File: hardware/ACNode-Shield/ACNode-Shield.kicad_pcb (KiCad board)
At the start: 2 copper layers, 50 x 50 mm, 15 parts, among them J1 MICRO_SD_HINGE, P1 CONN_NFC, P2 CONN_RELAY, P3 CONN_RGB_LED, P4 CONN_X6, P5 CONN_X7, P6 CONN_WS2812, Q1 PN2222A, SW1 SW_RST, SW2 SW_BTN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

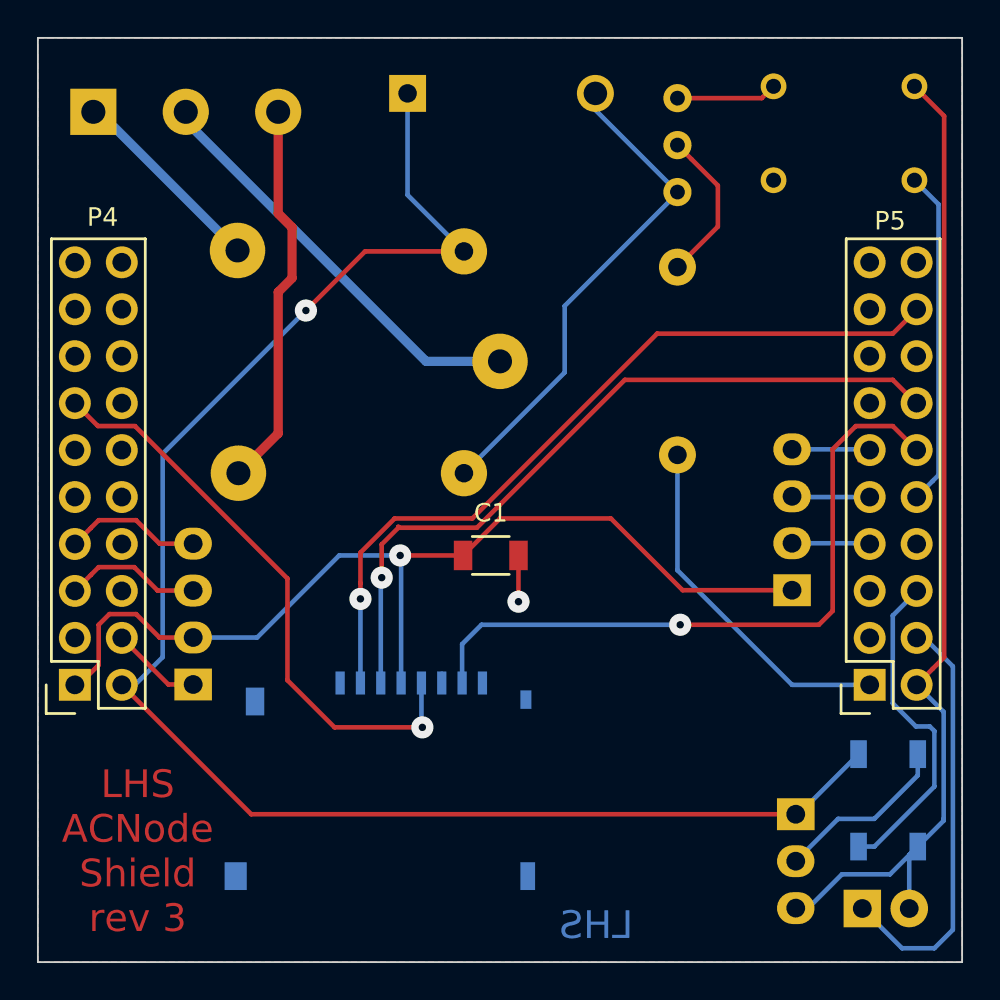
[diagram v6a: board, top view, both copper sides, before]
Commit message: Reversed contacts on the SD card connector - it should work now.
Bumped revision of the board to 4.
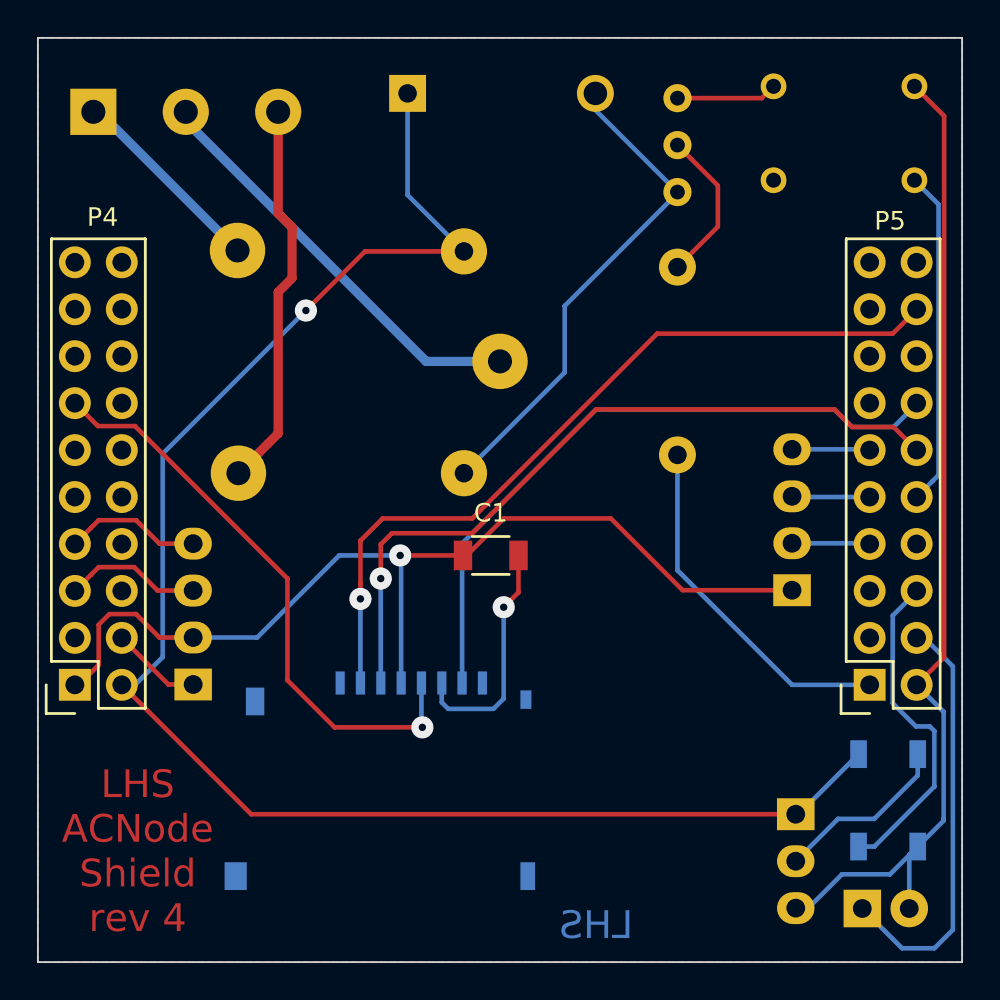
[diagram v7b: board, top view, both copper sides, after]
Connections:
- J1 pad 3: PQ3 -> PQ2
- J1 pad 7: PQ2 -> PQ3
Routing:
- net GND: track 69.8 -> 80.1 mm
- net PQ3: track 42.2 -> 36.1 mm, vias 1 -> 0
- net PQ2: track 37.2 -> 41.8 mm
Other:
- board text added: "LHS ACNode Shield rev 4"
- board text removed: "LHS ACNode Shield rev 3"
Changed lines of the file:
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@@
     (thickness 1.6)
     (drawings 6)
-    (tracks 174)
+    (tracks 176)
     (zones 0)
     (modules 15)
@@
       (net 9 PQ1))
     (pad 3 smd rect (at -3.55 7.1) (size 0.5 1.25) (layers B.Cu B.Paste B.Mask)
-      (net 8 PQ3))
+      (net 6 PQ2))
     (pad 4 smd rect (at -4.65 7.1) (size 0.5 1.25) (layers B.Cu B.Paste B.Mask)
       (net 1 +3.3v))
@@
       (net 2 GND))
     (pad 7 smd rect (at -7.95 7.1) (size 0.5 1.25) (layers B.Cu B.Paste B.Mask)
-      (net 6 PQ2))
+      (net 8 PQ3))
     (pad 8 smd rect (at -9.05 7.1) (size 0.5 1.25) (layers B.Cu B.Paste B.Mask)
       (net 5 "Net-(J1-Pad8)"))
@@
     )
   )
-  (gr_text "LHS\nACNode\nShield\nrev 3" (at 17.4 56) (layer F.Cu)
+  (gr_text "LHS\nACNode\nShield\nrev 4" (at 17.4 56) (layer F.Cu)
     (effects (font (size 1.5 1.5) (thickness 0.3)))
   )
@@
   (segment (start 23.86 44.44) (end 28.3 40) (width 0.25) (layer B.Cu) (net 1))
   (segment (start 28.3 40) (end 31.6 40) (width 0.25) (layer B.Cu) (net 1))
-  (segment (start 31.6 40) (end 35 40) (width 0.25) (layer F.Cu) (net 1))
+  (segment (start 31.6 40) (end 35.2 40) (width 0.25) (layer F.Cu) (net 1))
   (via (at 31.6 40) (size 1.2) (drill 0.4) (layers F.Cu B.Cu) (net 1))
   (segment (start 20.4 44.44) (end 20.56 44.44) (width 0.25) (layer B.Cu) (net 1))
   (segment (start 52.8 41.88) (end 46.88 41.88) (width 0.25) (layer F.Cu) (net 1))
   (segment (start 46.88 41.88) (end 43 38) (width 0.25) (layer F.Cu) (net 1))
-  (segment (start 43 38) (end 37 38) (width 0.25) (layer F.Cu) (net 1))
-  (segment (start 37 38) (end 35 40) (width 0.25) (layer F.Cu) (net 1))
+  (segment (start 43 38) (end 37.2 38) (width 0.25) (layer F.Cu) (net 1))
+  (segment (start 37.2 38) (end 35.2 40) (width 0.25) (layer F.Cu) (net 1))
   (segment (start 31.65 46.9) (end 31.65 46.35) (width 0.25) (layer B.Cu) (net 1))
   (segment (start 20.4 44.44) (end 18.57913 44.44) (width 0.25) (layer F.Cu) (net 1))
@@
   (segment (start 15.288601 45.924999) (end 14.2136 47) (width 0.25) (layer F.Cu) (net 1))
   (segment (start 14.2136 47) (end 14 47) (width 0.25) (layer F.Cu) (net 1))
-  (segment (start 38 42.5) (end 38 40) (width 0.25) (layer F.Cu) (net 2))
-  (via (at 38 42.5) (size 1.2) (drill 0.4) (layers F.Cu B.Cu) (net 2))
+  (segment (start 33.85 46.9) (end 33.85 47.95) (width 0.25) (layer B.Cu) (net 2))
+  (segment (start 38 42) (end 38 40) (width 0.25) (layer F.Cu) (net 2))
+  (segment (start 37.2 42.8) (end 38 42) (width 0.25) (layer F.Cu) (net 2))
+  (via (at 37.2 42.8) (size 1.2) (drill 0.4) (layers F.Cu B.Cu) (net 2))
+  (segment (start 37.2 47.75) (end 37.2 42.8) (width 0.25) (layer B.Cu) (net 2))
+  (segment (start 36.65 48.3) (end 37.2 47.75) (width 0.25) (layer B.Cu) (net 2))
+  (segment (start 34.2 48.3) (end 36.65 48.3) (width 0.25) (layer B.Cu) (net 2))
+  (segment (start 33.85 47.95) (end 34.2 48.3) (width 0.25) (layer B.Cu) (net 2))
   (segment (start 33.85 46.9) (end 33.85 46.4) (width 0.25) (layer B.Cu) (net 2))
   (segment (start 53 59.08) (end 52.58 59.08) (width 0.25) (layer B.Cu) (net 2))
@@
   (segment (start 53 54) (end 53.15044 54) (width 0.25) (layer B.Cu) (net 4))
   (segment (start 53.15044 54) (end 56.3998 50.75064) (width 0.25) (layer B.Cu) (net 4))
-  (segment (start 34.95 46.9) (end 34.95 44.8) (width 0.25) (layer B.Cu) (net 6))
-  (segment (start 58.25 33) (end 56.25 33) (width 0.25) (layer F.Cu) (net 6))
-  (segment (start 56.25 33) (end 55 34.25) (width 0.25) (layer F.Cu) (net 6))
-  (segment (start 55 34.25) (end 55 43) (width 0.25) (layer F.Cu) (net 6))
-  (segment (start 55 43) (end 54.25 43.75) (width 0.25) (layer F.Cu) (net 6))
-  (segment (start 54.25 43.75) (end 46.75 43.75) (width 0.25) (layer F.Cu) (net 6))
-  (segment (start 58.25 33) (end 59.54 34.29) (width 0.25) (layer F.Cu) (net 6))
-  (via (at 46.75 43.75) (size 1.2) (drill 0.4) (layers F.Cu B.Cu) (net 6))
-  (segment (start 36 43.75) (end 46.75 43.75) (width 0.25) (layer B.Cu) (net 6))
-  (segment (start 34.95 44.8) (end 36 43.75) (width 0.25) (layer B.Cu) (net 6))
+  (segment (start 30.55 46.9) (end 30.55 41.25) (width 0.25) (layer B.Cu) (net 6))
+  (segment (start 58.29 33.05) (end 59.54 34.3) (width 0.25) (layer F.Cu) (net 6))
+  (segment (start 56.05 33.05) (end 58.29 33.05) (width 0.25) (layer F.Cu) (net 6))
+  (segment (start 55.1 32.1) (end 56.05 33.05) (width 0.25) (layer F.Cu) (net 6))
+  (segment (start 42.2 32.1) (end 55.1 32.1) (width 0.25) (layer F.Cu) (net 6))
+  (segment (start 35.5 38.8) (end 42.2 32.1) (width 0.25) (layer F.Cu) (net 6))
+  (segment (start 31.15 38.8) (end 35.5 38.8) (width 0.25) (layer F.Cu) (net 6))
+  (segment (start 30.55 39.4) (end 31.15 38.8) (width 0.25) (layer F.Cu) (net 6))
+  (segment (start 30.55 40) (end 30.55 39.4) (width 0.25) (layer F.Cu) (net 6))
+  (segment (start 30.55 41.25) (end 30.55 40) (width 0.25) (layer F.Cu) (net 6))
+  (via (at 30.55 41.25) (size 1.2) (drill 0.4) (layers F.Cu B.Cu) (net 6))
   (segment (start 59.54 34.3) (end 59.54 34.29) (width 0.25) (layer F.Cu) (net 6))
+  (segment (start 30.55 46.45) (end 30.55 46.9) (width 0.25) (layer B.Cu) (net 6))
+  (segment (start 30.55 46.9) (end 30.55 46.45) (width 0.25) (layer B.Cu) (net 6))
+  (segment (start 30.55 46.9) (end 30.55 46.4) (width 0.25) (layer B.Cu) (net 6))
   (segment (start 32.8 49.3) (end 28.05 49.3) (width 0.25) (layer F.Cu) (net 7))
   (segment (start 25.5 41.25) (end 25.5 46.75) (width 0.25) (layer F.Cu) (net 7))
@@
   (segment (start 32.75 47.25) (end 32.75 46.9) (width 0.25) (layer B.Cu) (net 7))
   (segment (start 32.75 46.9) (end 32.75 46.5) (width 0.25) (layer B.Cu) (net 7))
-  (segment (start 30.55 46.9) (end 30.55 41.25) (width 0.25) (layer B.Cu) (net 8))
-  (segment (start 30.6 39.4) (end 31.5 38.5) (width 0.25) (layer F.Cu) (net 8))
-  (segment (start 30.6 41.2) (end 30.6 39.4) (width 0.25) (layer F.Cu) (net 8))
-  (via (at 30.6 41.2) (size 1.2) (drill 0.4) (layers F.Cu B.Cu) (net 8))
-  (segment (start 30.55 41.25) (end 30.6 41.2) (width 0.25) (layer B.Cu) (net 8))
-  (segment (start 31.5 38.5) (end 31.5 38.450002) (width 0.25) (layer F.Cu) (net 8))
-  (segment (start 31.5 38.450002) (end 31.5 38.5) (width 0.25) (layer F.Cu) (net 8))
-  (segment (start 35.75 38.5) (end 31.5 38.5) (width 0.25) (layer F.Cu) (net 8))
-  (segment (start 59.51 31.76) (end 58.25 30.5) (width 0.25) (layer F.Cu) (net 8))
-  (segment (start 58.25 30.5) (end 43.75 30.5) (width 0.25) (layer F.Cu) (net 8))
-  (segment (start 43.75 30.5) (end 35.75 38.5) (width 0.25) (layer F.Cu) (net 8))
-  (segment (start 31.5 38.5) (end 31.5 38.5) (width 0.25) (layer F.Cu) (net 8))
-  (segment (start 30.55 46.45) (end 30.55 46.9) (width 0.25) (layer B.Cu) (net 8))
-  (segment (start 30.55 46.9) (end 30.55 46.45) (width 0.25) (layer B.Cu) (net 8))
+  (segment (start 59.54 31.76) (end 59.54 31.81) (width 0.25) (layer B.Cu) (net 8))
+  (segment (start 59.54 31.81) (end 58.3 33.05) (width 0.25) (layer B.Cu) (net 8))
+  (segment (start 34.95 39.35) (end 34.95 46.9) (width 0.25) (layer B.Cu) (net 8))
+  (segment (start 42.2 32.1) (end 34.95 39.35) (width 0.25) (layer B.Cu) (net 8))
+  (segment (start 55.1 32.1) (end 42.2 32.1) (width 0.25) (layer B.Cu) (net 8))
+  (segment (start 56.05 33.05) (end 55.1 32.1) (width 0.25) (layer B.Cu) (net 8))
+  (segment (start 58.3 33.05) (end 56.05 33.05) (width 0.25) (layer B.Cu) (net 8))
   (segment (start 59.54 31.76) (end 59.51 31.76) (width 0.25) (layer F.Cu) (net 8))
-  (segment (start 30.55 46.9) (end 30.55 46.4) (width 0.25) (layer B.Cu) (net 8))
-  (segment (start 31.3 38) (end 29.45 39.85) (width 0.25) (layer F.Cu) (net 9))
+  (segment (start 30.65 38) (end 29.45 39.2) (width 0.25) (layer F.Cu) (net 9))
   (segment (start 29.45 42.35) (end 29.45 41.501472) (width 0.25) (layer F.Cu) (net 9))
-  (segment (start 29.45 41.501472) (end 29.45 39.85) (width 0.25) (layer F.Cu) (net 9))
+  (segment (start 29.45 41.501472) (end 29.45 39.2) (width 0.25) (layer F.Cu) (net 9))
   (segment (start 29.45 46.9) (end 29.45 42.35) (width 0.25) (layer B.Cu) (net 9))
   (via (at 29.45 42.35) (size 1.2) (drill 0.4) (layers F.Cu B.Cu) (net 9))
   (segment (start 58.25 28) (end 45.5 28) (width 0.25) (layer F.Cu) (net 9))
   (segment (start 45.5 28) (end 35.5 38) (width 0.25) (layer F.Cu) (net 9))
-  (segment (start 35.5 38) (end 31.3 38) (width 0.25) (layer F.Cu) (net 9))
+  (segment (start 35.5 38) (end 30.65 38) (width 0.25) (layer F.Cu) (net 9))
   (segment (start 59.54 26.71) (end 58.25 28) (width 0.25) (layer F.Cu) (net 9))
   (segment (start 59.54 26.68) (end 59.54 26.71) (width 0.25) (layer F.Cu) (net 9))
